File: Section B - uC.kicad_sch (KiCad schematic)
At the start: 8 parts, among them J1 Conn_ARM_SWD_TagConnect_TC203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, U1 ATtiny204-SS

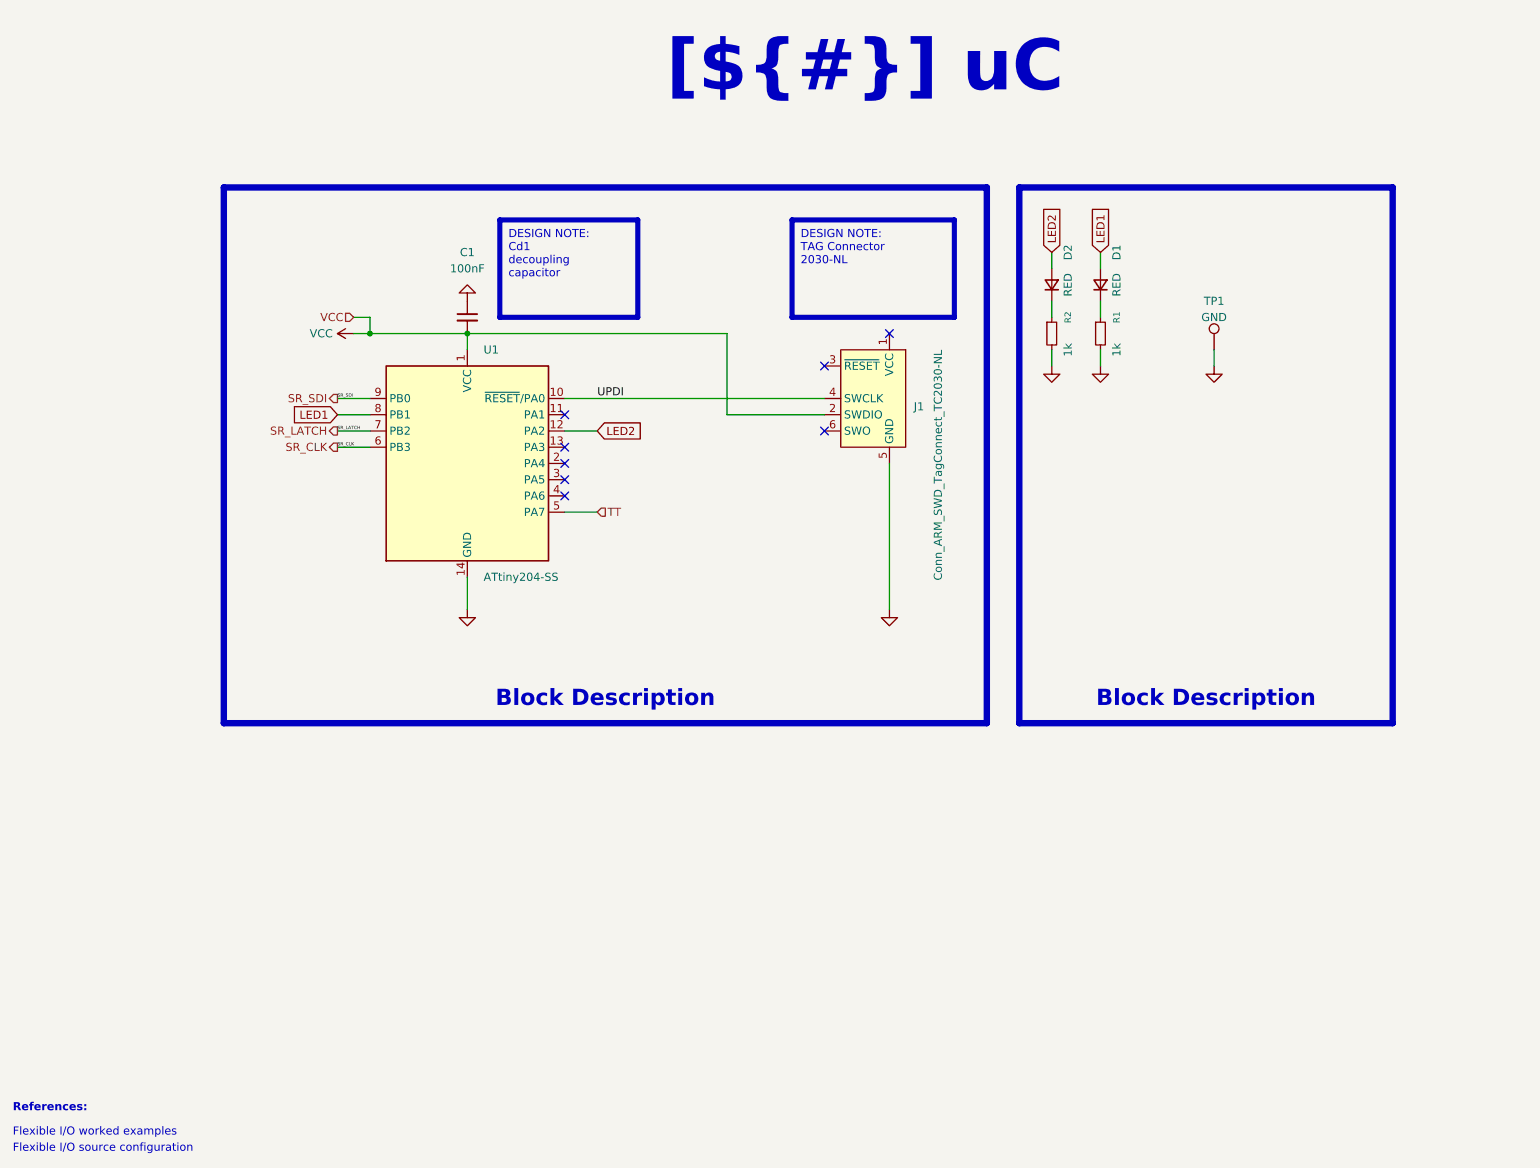
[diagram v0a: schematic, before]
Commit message: screw interface update - changed pinout
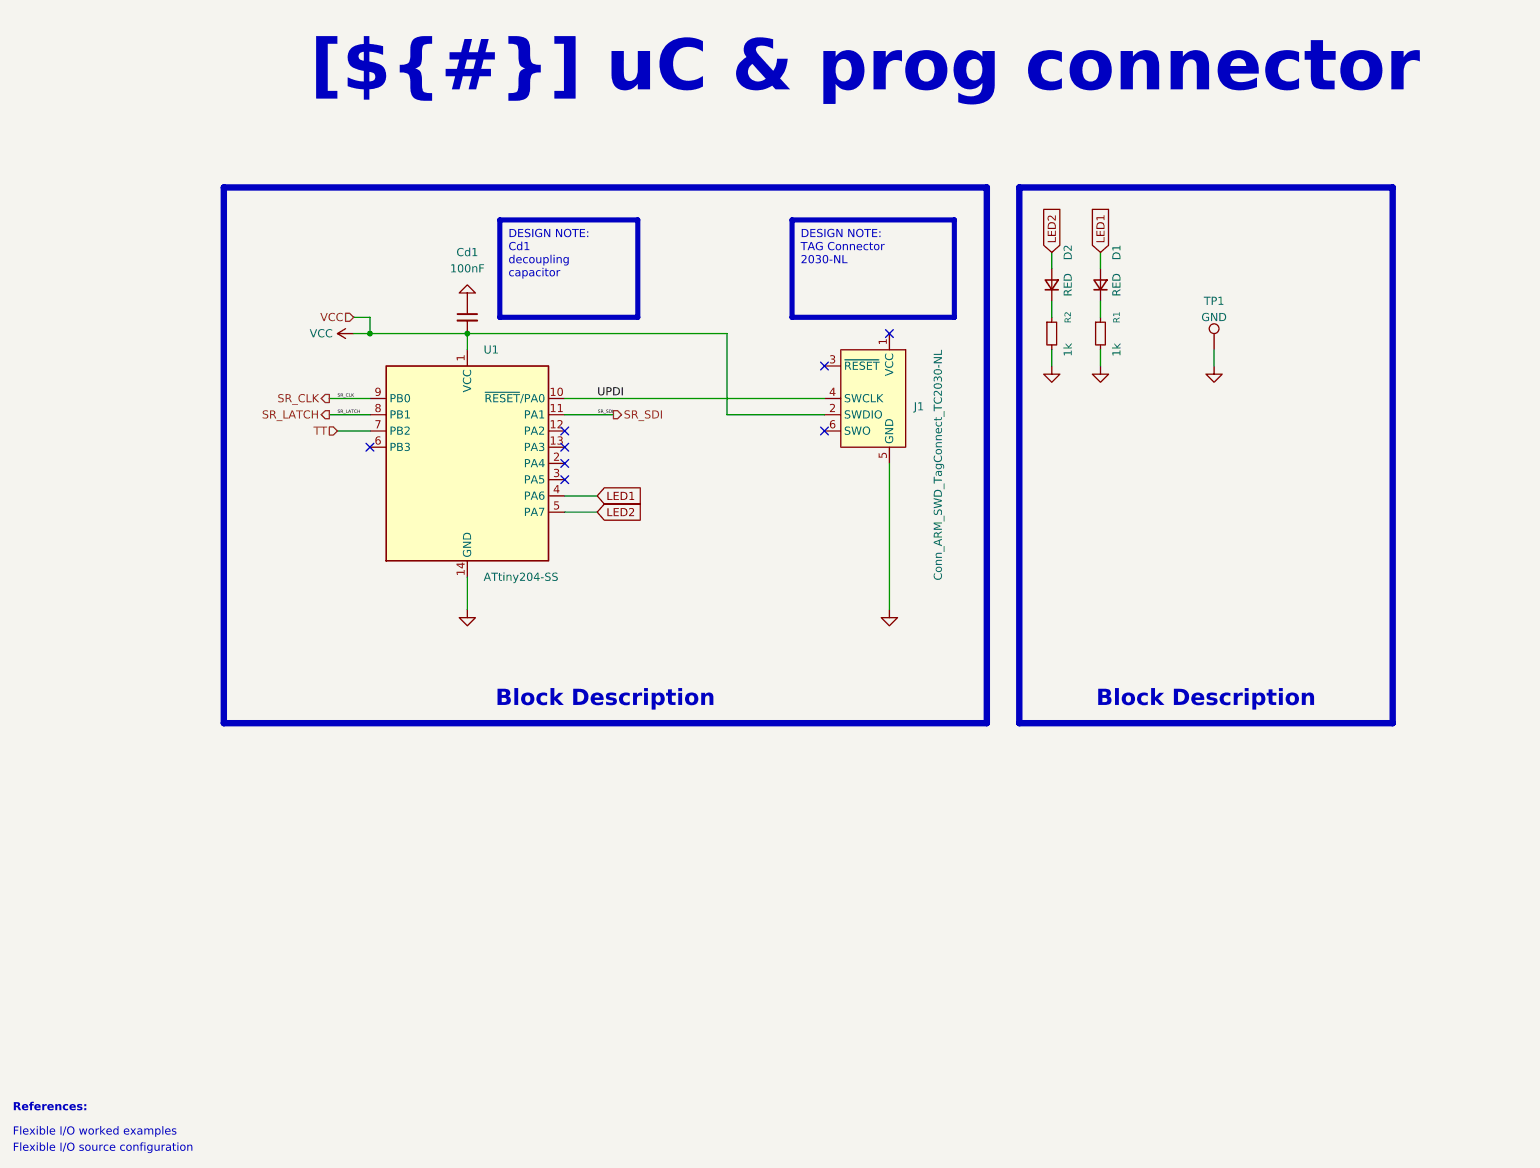
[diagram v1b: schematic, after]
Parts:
- renumbered C1 to Cd1
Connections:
- net LED1: now also U1.4 (PA6); no longer U1.8 (PB1)
- net LED2: now also U1.5 (PA7); no longer U1.12 (PA2)
- net SR_CLK: now also U1.9 (PB0); no longer U1.6 (PB3)
- net SR_LATCH: now also U1.8 (PB1); no longer U1.7 (PB2)
- net SR_SDI: now also U1.11 (PA1); no longer U1.9 (PB0)
- net TT: now also U1.7 (PB2); no longer U1.5 (PA7)
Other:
- title: uC -> uC & prog connector

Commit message: [CFG] Configuration update, added bom information fields
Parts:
- TP1: BOM_INFO (none) -> N/A; BOM_STATUS (none) -> OK
- U1: BOM_INFO (none) -> TME have; BOM_STATUS (none) -> OK

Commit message: bom update, qr-code added
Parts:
- Cd1, D1, D2, R1, R2: BOM_INFO (none) -> AIDATEK A0; BOM_STATUS (none) -> OK
- TP1: BOM_STATUS OK -> N/A
- U1: BOM_INFO TME have -> AIDATEK A1
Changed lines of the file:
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@@
 			)
 		)
-		(property "BOM_INFO" ""
+		(property "BOM_INFO" "AIDATEK A0"
 			(at 177.8 66.04 90)
 			(effects
@@
 			)
 		)
-		(property "BOM_STATUS" ""
+		(property "BOM_STATUS" "OK"
 			(at 177.8 66.04 90)
 			(effects
@@
 			)
 		)
-		(property "BOM_INFO" "TME have"
+		(property "BOM_INFO" "AIDATEK A1"
 			(at 86.36 86.36 0)
 			(effects
@@
 			)
 		)
-		(property "BOM_INFO" ""
+		(property "BOM_INFO" "AIDATEK A0"
 			(at 185.42 66.04 90)
 			(effects
@@
 			)
 		)
-		(property "BOM_STATUS" ""
+		(property "BOM_STATUS" "OK"
 			(at 185.42 66.04 90)
 			(effects
@@
 			)
 		)
-		(property "BOM_INFO" ""
+		(property "BOM_INFO" "AIDATEK A0"
 			(at 86.36 63.5 0)
 			(effects
@@
 			)
 		)
-		(property "BOM_STATUS" ""
+		(property "BOM_STATUS" "OK"
 			(at 86.36 63.5 0)
 			(effects
@@
 			)
 		)
-		(property "BOM_STATUS" "OK"
+		(property "BOM_STATUS" "N/A"
 			(at 203.2 68.58 0)
 			(effects
@@
 			)
 		)
-		(property "BOM_INFO" ""
+		(property "BOM_INFO" "AIDATEK A0"
 			(at 177.8 58.42 0)
 			(effects
@@
 			)
 		)
-		(property "BOM_STATUS" ""
+		(property "BOM_STATUS" "OK"
 			(at 177.8 58.42 0)
 			(effects
@@
 			)
 		)
-		(property "BOM_INFO" ""
+		(property "BOM_INFO" "AIDATEK A0"
 			(at 185.42 58.42 0)
 			(effects
@@
 			)
 		)
-		(property "BOM_STATUS" ""
+		(property "BOM_STATUS" "OK"
 			(at 185.42 58.42 0)
 			(effects

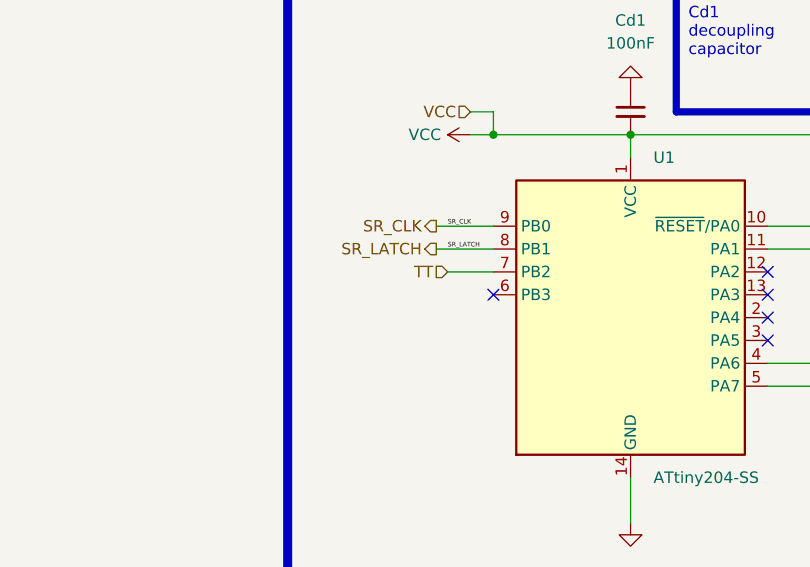
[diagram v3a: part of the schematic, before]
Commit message: [sch] added R3 to prevent high current drain from cap touch chip
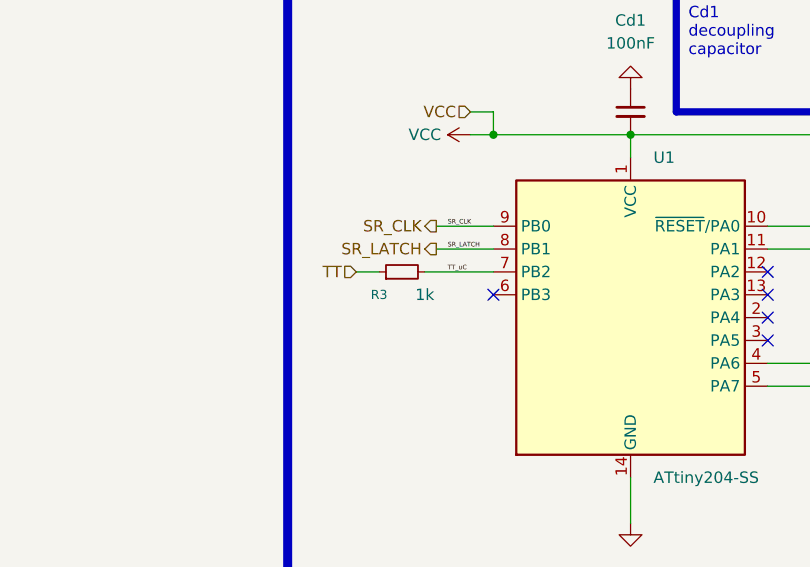
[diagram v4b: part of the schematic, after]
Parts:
- added R3: 1k, Resistor_SMD:R_0805_2012Metric, symbol Device:R_Small
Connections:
- net TT: now also R3.1; no longer U1.7 (PB2)
- new net TT_uC: R3.2, U1.7 (PB2)
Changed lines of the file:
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@@
+	(wire
+		(pts
+			(xy 63.5 81.28) (xy 71.12 81.28)
+		)
+		(stroke
+			(width 0)
+			(type default)
+		)
+	)
 	(wire
 		(pts
@@
 	(wire
 		(pts
-			(xy 71.12 81.28) (xy 66.04 81.28)
+			(xy 64.77 78.74) (xy 71.12 78.74)
 		)
 		(stroke
@@
 	(wire
 		(pts
-			(xy 64.77 78.74) (xy 71.12 78.74)
+			(xy 55.88 81.28) (xy 58.42 81.28)
 		)
 		(stroke
@@
 		)
 	)
+	(label "TT_uC"
+		(at 66.04 81.28 0)
+		(effects
+			(font
+				(size 0.508 0.508)
+			)
+			(justify left bottom)
+		)
+	)
 	(label "SR_SDI"
 		(at 109.22 78.74 180)
@@
 	(hierarchical_label "TT"
 		(shape input)
-		(at 66.04 81.28 180)
+		(at 55.88 81.28 180)
 		(effects
 			(font
@@
 					(unit 1)
 				)
+			)
+		)
+	)
+	(symbol
+		(lib_id "Device:R_Small")
+		(at 60.96 81.28 90)
+		(unit 1)
+		(exclude_from_sim no)
+		(in_bom yes)
+		(on_board yes)
+		(dnp no)
+		(property "Reference" "R3"
+			(at 58.42 83.82 90)
+			(effects
+				(font
+					(size 1.016 1.016)
+				)
+			)
+		)
+		(property "Value" "1k"
+			(at 63.5 83.82 90)
+			(effects
+				(font
+					(size 1.27 1.27)
+				)
+			)
+		)
+		(property "Footprint" "Resistor_SMD:R_0805_2012Metric"
+			(at 60.96 81.28 0)
+			(effects
+				(font
+					(size 1.27 1.27)
+				)
+				(hide yes)
+			)
+		)
+		(property "Datasheet" "~"
+			(at 60.96 81.28 0)
+			(effects
+				(font
+					(size 1.27 1.27)
+				)
+				(hide yes)
+			)
+		)
+		(property "Description" "Resistor, small symbol"
+			(at 60.96 81.28 0)
+			(effects
+				(font
+					(size 1.27 1.27)
+				)
+				(hide yes)
+			)
+		)
+		(property "BOM_INFO" "AIDATEK A0"
+			(at 60.96 81.28 90)
+			(effects
+				(font
+					(size 1.27 1.27)
+				)
+				(hide yes)
+			)
+		)
+		(property "BOM_STATUS" "OK"
+			(at 60.96 81.28 90)
+			(effects
+				(font
+					(size 1.27 1.27)
+				)
+				(hide yes)
+			)
+		)
+		(property "Config" ""
+			(at 60.96 81.28 90)
+			(effects
+				(font
+					(size 1.27 1.27)
+				)
+				(hide yes)
+			)
+		)
+		(property "Manufacturer" ""
+			(at 60.96 81.28 90)
+			(effects
+				(font
+					(size 1.27 1.27)
+				)
+				(hide yes)
+			)
+		)
+		(property "Manufacturer Part Number" ""
+			(at 60.96 81.28 90)
+			(effects
+				(font
+					(size 1.27 1.27)
+				)
+				(hide yes)
+			)
+		)
+		(pin "1"
+		)
+		(pin "2"
+		)
+		(instances
+			(project "Sienkiewicz_TOUCH"
+				(path "/f9e05184-c88b-4a88-ae9c-ab2bdb32be7c/c5103ceb-5325-4a84-a025-9638a412984e/e744f3ce-03a6-44a6-8792-1447ef232b9a"
+					(reference "R3")
+					(unit 1)
+				)

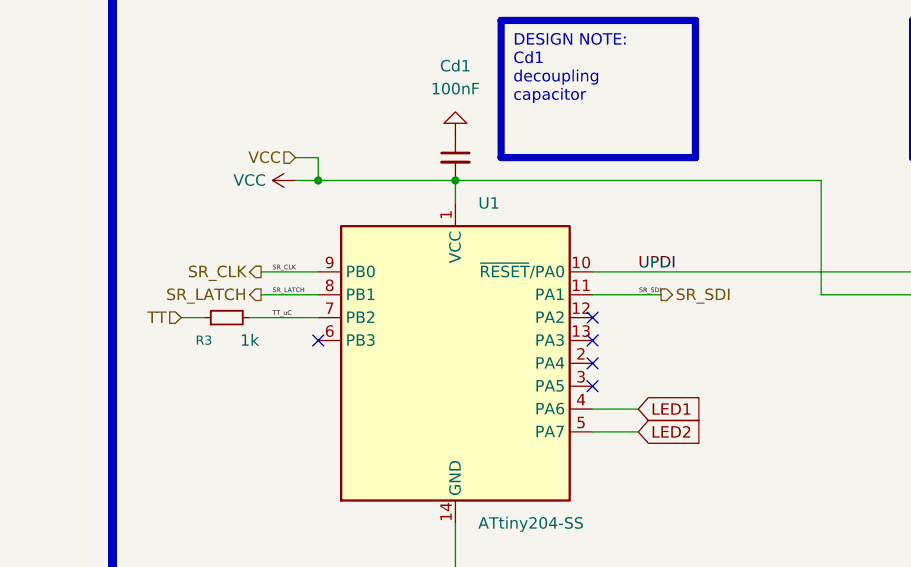
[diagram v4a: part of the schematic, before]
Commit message: [pcb] board outline/connection changed / back compatibility not possible
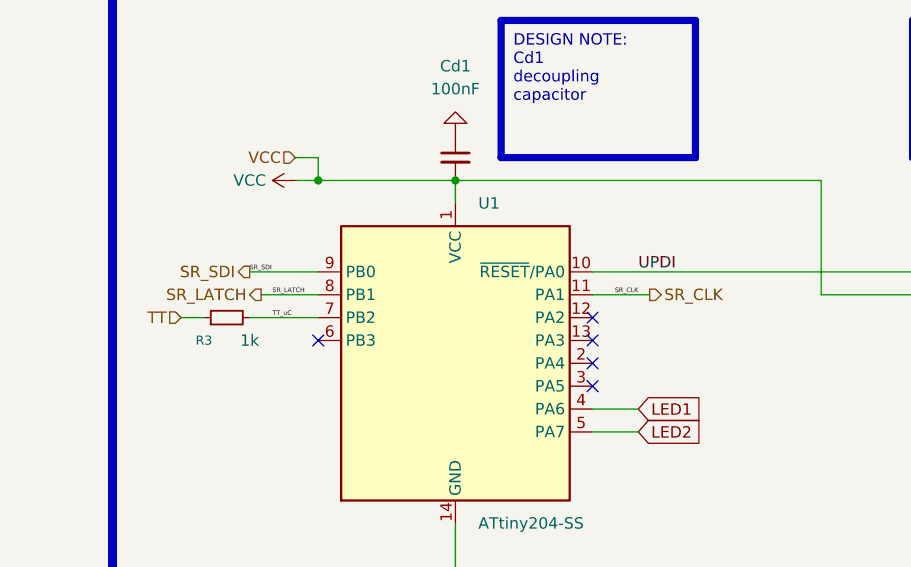
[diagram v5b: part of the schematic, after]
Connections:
- net SR_CLK: now also U1.11 (PA1); no longer U1.9 (PB0)
- net SR_SDI: now also U1.9 (PB0); no longer U1.11 (PA1)
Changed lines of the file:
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@@
 	(wire
 		(pts
-			(xy 101.6 78.74) (xy 109.22 78.74)
+			(xy 71.12 76.2) (xy 63.5 76.2)
 		)
 		(stroke
@@
 	(wire
 		(pts
-			(xy 64.77 76.2) (xy 71.12 76.2)
+			(xy 107.95 78.74) (xy 101.6 78.74)
 		)
 		(stroke
@@
 	)
 	(label "SR_SDI"
-		(at 109.22 78.74 180)
+		(at 63.5 76.2 0)
 		(effects
 			(font
 				(size 0.508 0.508)
 			)
+			(justify left bottom)
+		)
+	)
+	(label "SR_CLK"
+		(at 106.68 78.74 180)
+		(effects
+			(font
+				(size 0.508 0.508)
+			)
 			(justify right bottom)
-		)
-	)
-	(label "SR_CLK"
-		(at 66.04 76.2 0)
-		(effects
-			(font
-				(size 0.508 0.508)
-			)
-			(justify left bottom)
 		)
 	)
@@
 	(hierarchical_label "SR_CLK"
 		(shape output)
-		(at 64.77 76.2 180)
+		(at 107.95 78.74 0)
 		(effects
 			(font
 				(size 1.27 1.27)
 			)
-			(justify right)
+			(justify left)
 		)
 	)
 	(hierarchical_label "SR_SDI"
 		(shape output)
-		(at 109.22 78.74 0)
+		(at 63.5 76.2 180)
 		(effects
 			(font
 				(size 1.27 1.27)
 			)
-			(justify left)
-		)
-	)
+			(justify right)
+		)
+	)

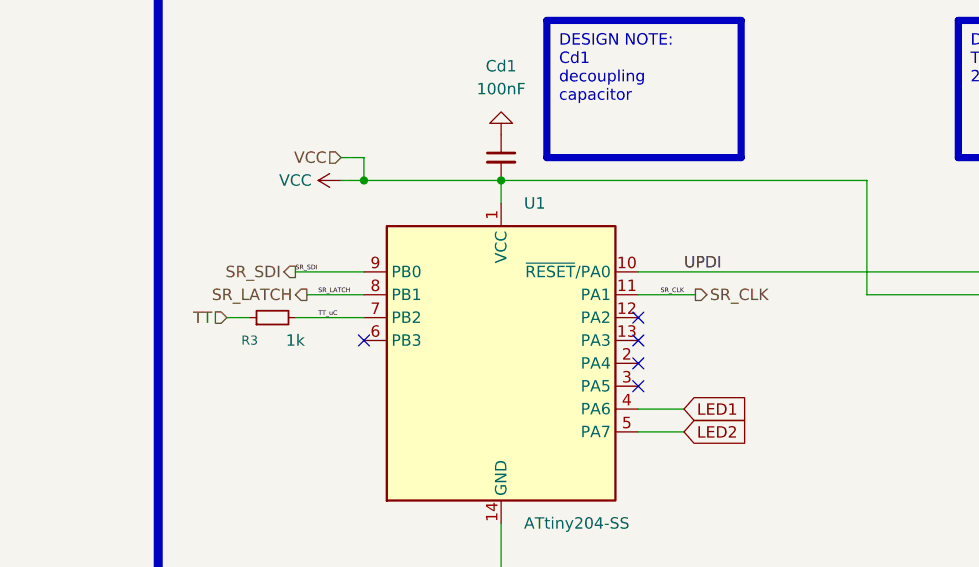
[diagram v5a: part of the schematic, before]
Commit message: reassign SR signals for clean design (fixes #4)
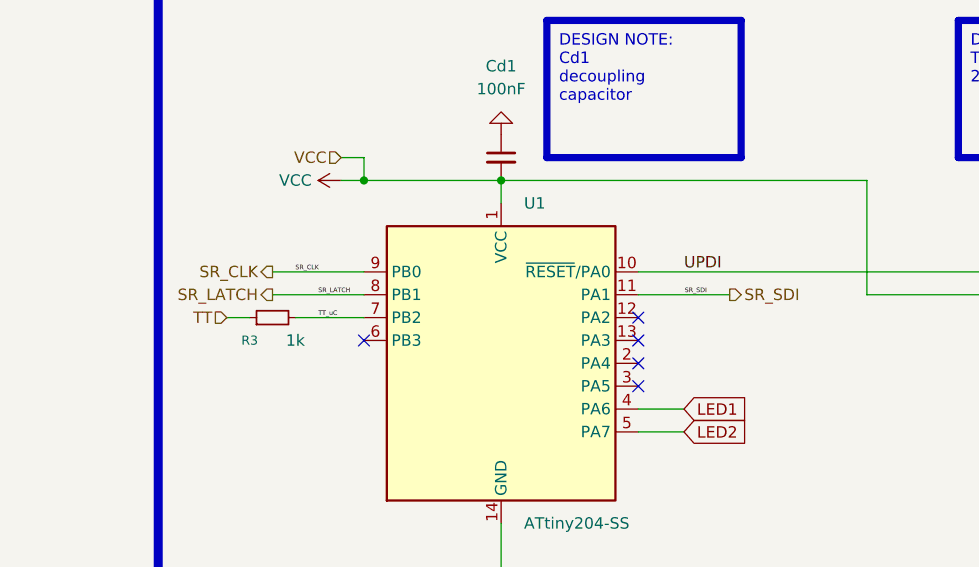
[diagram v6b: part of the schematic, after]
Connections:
- net SR_CLK: now also U1.9 (PB0); no longer U1.11 (PA1)
- net SR_SDI: now also U1.11 (PA1); no longer U1.9 (PB0)
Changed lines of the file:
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@@
-	(wire
-		(pts
-			(xy 71.12 76.2) (xy 63.5 76.2)
-		)
-		(stroke
-			(width 0)
-			(type default)
-		)
-	)
 	(wire
 		(pts
@@
 	(wire
 		(pts
+			(xy 101.6 78.74) (xy 111.76 78.74)
+		)
+		(stroke
+			(width 0)
+			(type default)
+		)
+	)
+	(wire
+		(pts
 			(xy 86.36 104.14) (xy 86.36 109.22)
 		)
@@
 	(wire
 		(pts
-			(xy 107.95 78.74) (xy 101.6 78.74)
+			(xy 60.96 76.2) (xy 71.12 76.2)
 		)
 		(stroke
@@
 	(wire
 		(pts
-			(xy 64.77 78.74) (xy 71.12 78.74)
+			(xy 60.96 78.74) (xy 71.12 78.74)
 		)
 		(stroke
@@
 	)
 	(label "SR_SDI"
+		(at 109.22 78.74 180)
+		(effects
+			(font
+				(size 0.508 0.508)
+			)
+			(justify right bottom)
+		)
+	)
+	(label "SR_CLK"
 		(at 63.5 76.2 0)
 		(effects
@@
 			)
 			(justify left bottom)
-		)
-	)
-	(label "SR_CLK"
-		(at 106.68 78.74 180)
-		(effects
-			(font
-				(size 0.508 0.508)
-			)
-			(justify right bottom)
 		)
 	)
@@
 	(hierarchical_label "SR_LATCH"
 		(shape output)
-		(at 64.77 78.74 180)
+		(at 60.96 78.74 180)
 		(effects
 			(font
@@
 	(hierarchical_label "SR_CLK"
 		(shape output)
-		(at 107.95 78.74 0)
+		(at 60.96 76.2 180)
 		(effects
 			(font
 				(size 1.27 1.27)
 			)
-			(justify left)
+			(justify right)
 		)
 	)
 	(hierarchical_label "SR_SDI"
 		(shape output)
-		(at 63.5 76.2 180)
+		(at 111.76 78.74 0)
 		(effects
 			(font
 				(size 1.27 1.27)
 			)
-			(justify right)
-		)
-	)
+			(justify left)
+		)
+	)
